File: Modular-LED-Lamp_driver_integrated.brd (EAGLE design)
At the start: 40 x 44 mm, 15 parts

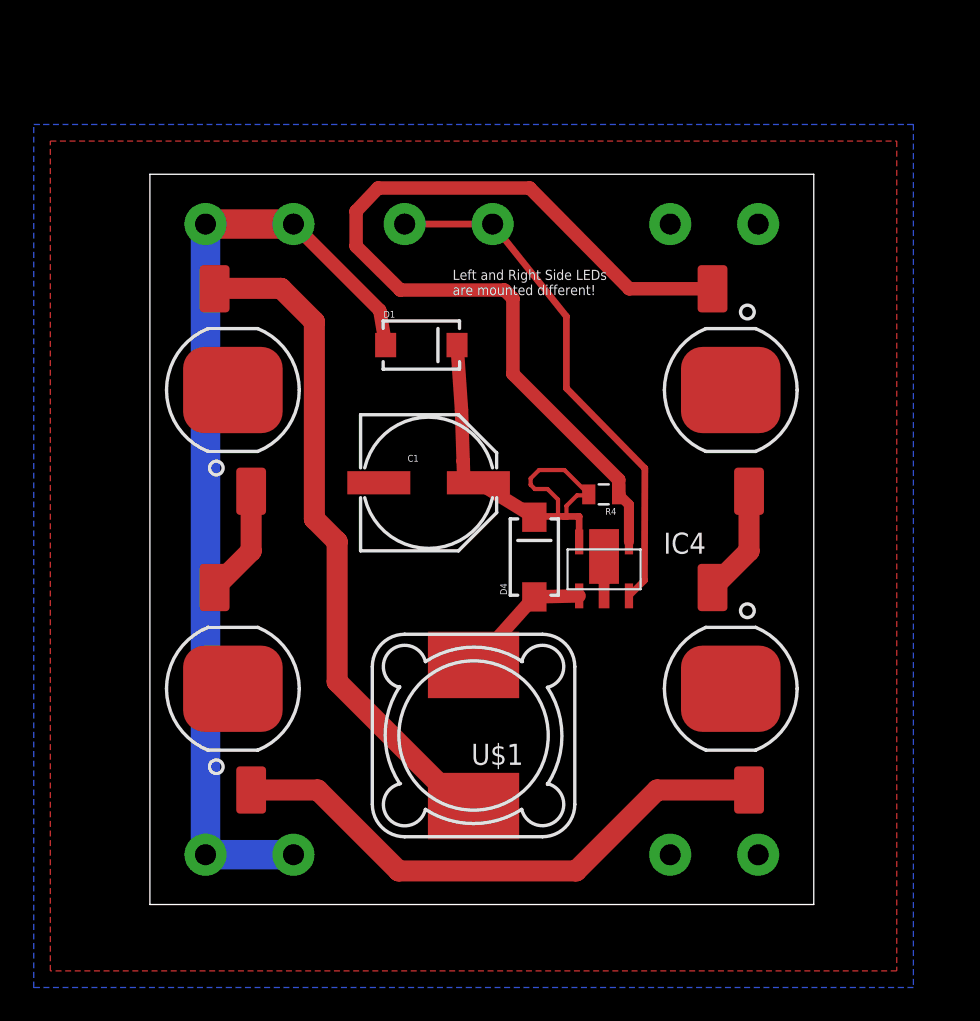
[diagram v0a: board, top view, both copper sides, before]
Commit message: changed outline to be bigger to disspate more heat, added footprint for 90° turned fuse holders, rounded edges
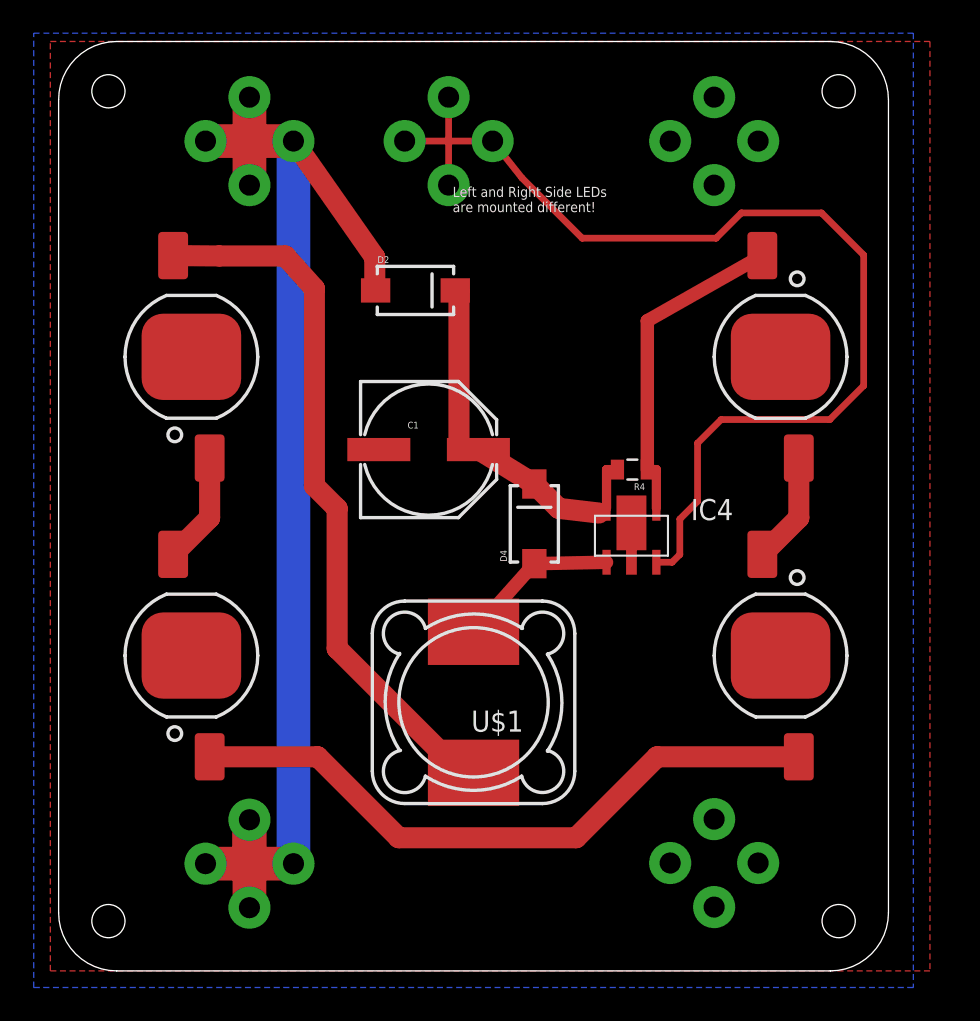
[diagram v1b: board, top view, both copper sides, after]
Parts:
- removed D1: B340A, SparkFun-DiscreteSemi:SMA-DIODE
- added D2: (no value), SparkFun-DiscreteSemi:SMA-DIODE-KIT
- added GND-CLIP1, GND-CLIP3: GND, timon-diverses:FUSE-HOLDER-5X20MM
- added PWM-CLIP1, VCC-CLIP1, VCC-CLIP3: FUSE-HOLDER-5X20MM, timon-diverses:FUSE-HOLDER-5X20MM
- R4: value 0.13 -> 0.33
- moved GND-CLIP 5.00 mm to (39.0, 47.0)
- moved PWM-CLIP 5.00 mm to (23.0, 47.0)
- moved VCC-CLIP 5.00 mm to (11.0, 47.0)
- moved LED-1 3.61 mm to (43.0, 34.0)
- moved LED-4 3.61 mm to (43.0, 16.0)
- moved LED-2 3.20 mm to (7.50, 16.0)
- moved LED-3 3.20 mm to (7.50, 34.0)
- moved IC4 2.61 mm to (32.5, 21.6)
- moved R4 2.28 mm to (34.1, 27.2)
- moved C1 2.00 mm to (21.8, 28.4)
- moved D4 2.00 mm to (28.2, 23.9)
- moved U$1 2.00 mm to (24.5, 13.2)
- moved VCC-CLIP2 0.54 mm to (11.0, 3.46)
- moved GND-CLIP2 0.50 mm to (39.0, 3.50)
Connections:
- net GND: now also GND-CLIP1.CLIP-INPUT1, GND-CLIP1.CLIP-INPUT2, GND-CLIP3.CLIP-INPUT1, GND-CLIP3.CLIP-INPUT2
- net PWM: now also PWM-CLIP1.CLIP-INPUT1, PWM-CLIP1.CLIP-INPUT2
- net VCC: now also D2.C; no longer D1.C
- net VCC-RAW: now also D2.A, VCC-CLIP1.CLIP-INPUT1, VCC-CLIP1.CLIP-INPUT2, VCC-CLIP3.CLIP-INPUT1, VCC-CLIP3.CLIP-INPUT2; no longer D1.A
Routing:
- net LED+: track 55.0 -> 19.8 mm
- net PWM: track 31.6 -> 65.4 mm
- net VCC-RAW: track 58.1 -> 78.0 mm
- net N$2: track 34.0 -> 39.5 mm
- net VCC: track 27.6 -> 23.0 mm
- net LED-: track 40.4 -> 43.0 mm
- net N$1: track 8.20 -> 9.85 mm
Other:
- board size 40 x 44 mm -> 50 x 56 mm

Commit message: updated integrated driver module to be 1W instead of 3W
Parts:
- R4: value 0.33 -> 0.3; device SparkFun-Resistors:0805 -> SparkFun-Resistors:1206
- moved R4 0.51 mm to (34.1, 27.7)
- renumbered U$1 to INDUCTOR
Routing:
- net VCC-RAW: track 78.0 -> 89.2 mm
- net LED+: track 19.8 -> 18.8 mm
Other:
- outline, holes or cut-outs redrawn
- board text added: "+"
- board text added: "-"
- board text added: "GND"
- board text added: "LED+"
- board text added: "LED-"
- board text added: "PT4115"
- board text added: "PWM"
- board text added: "Sense"
- board text added: "VCC"

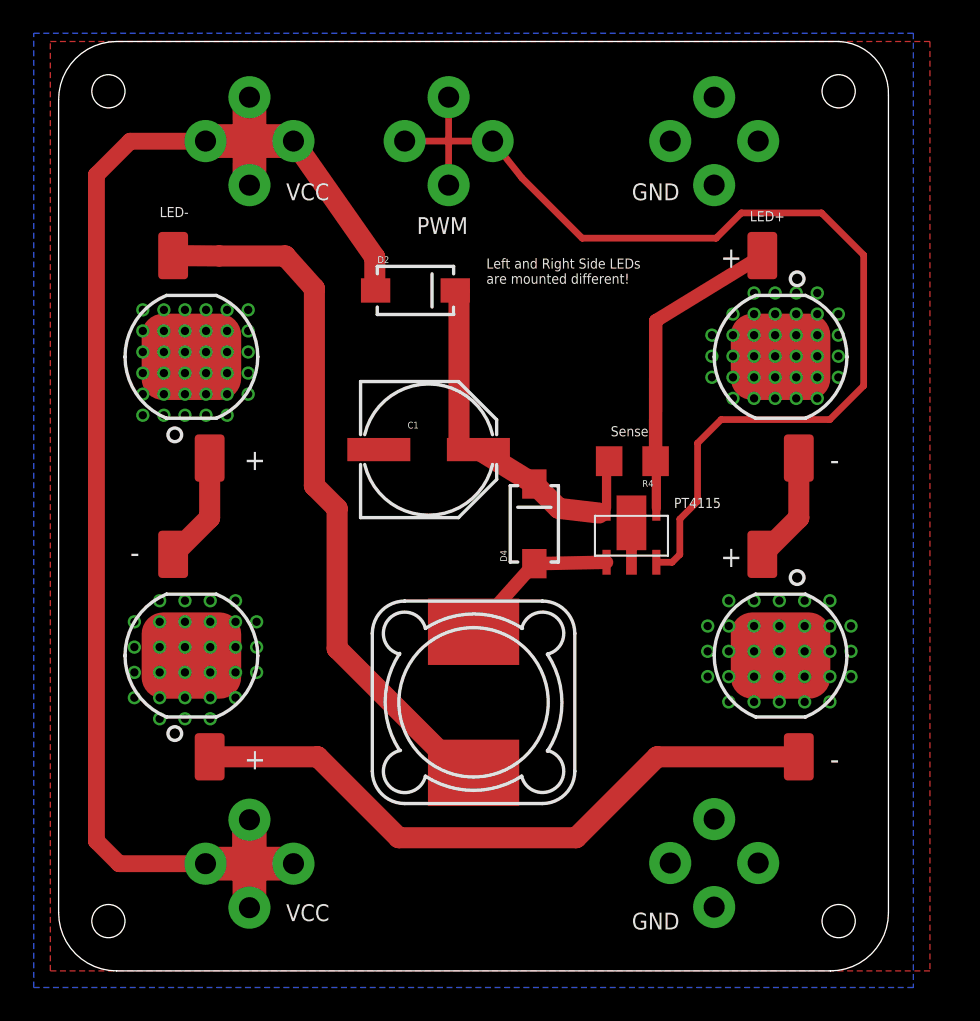
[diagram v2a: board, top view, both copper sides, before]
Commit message: fixed issued with PWM rod causing short circuit when two boards are mounted with one being reversed. Added PDF for schematic and board.
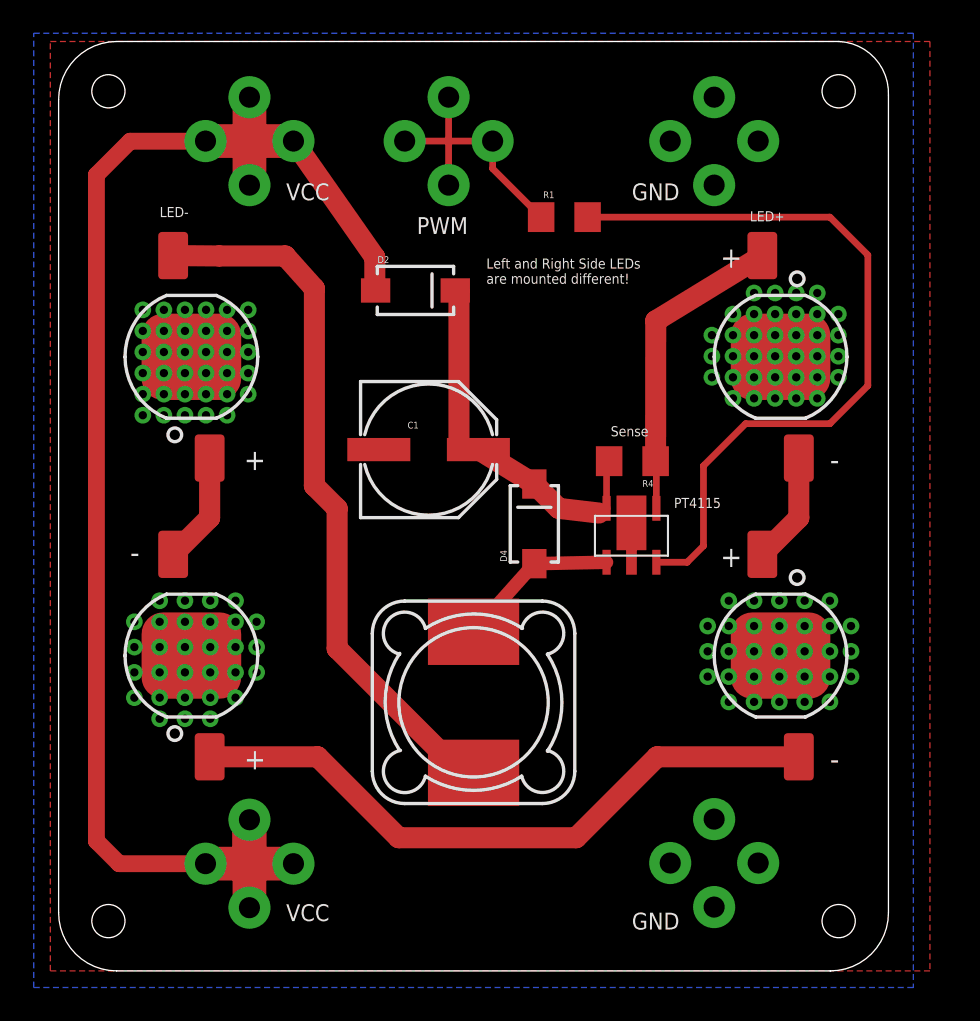
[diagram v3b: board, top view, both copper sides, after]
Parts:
- added R1: 2k, SparkFun-Resistors:1206
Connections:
- new net N$5: IC4.3, R1.2
- net PWM: now also R1.1; no longer IC4.3
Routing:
- net PWM: track 65.4 -> 16.5 mm
- net N$5: track 0.00 -> 45.7 mm

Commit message: Added BOM, updated schematic and board for integrated variant
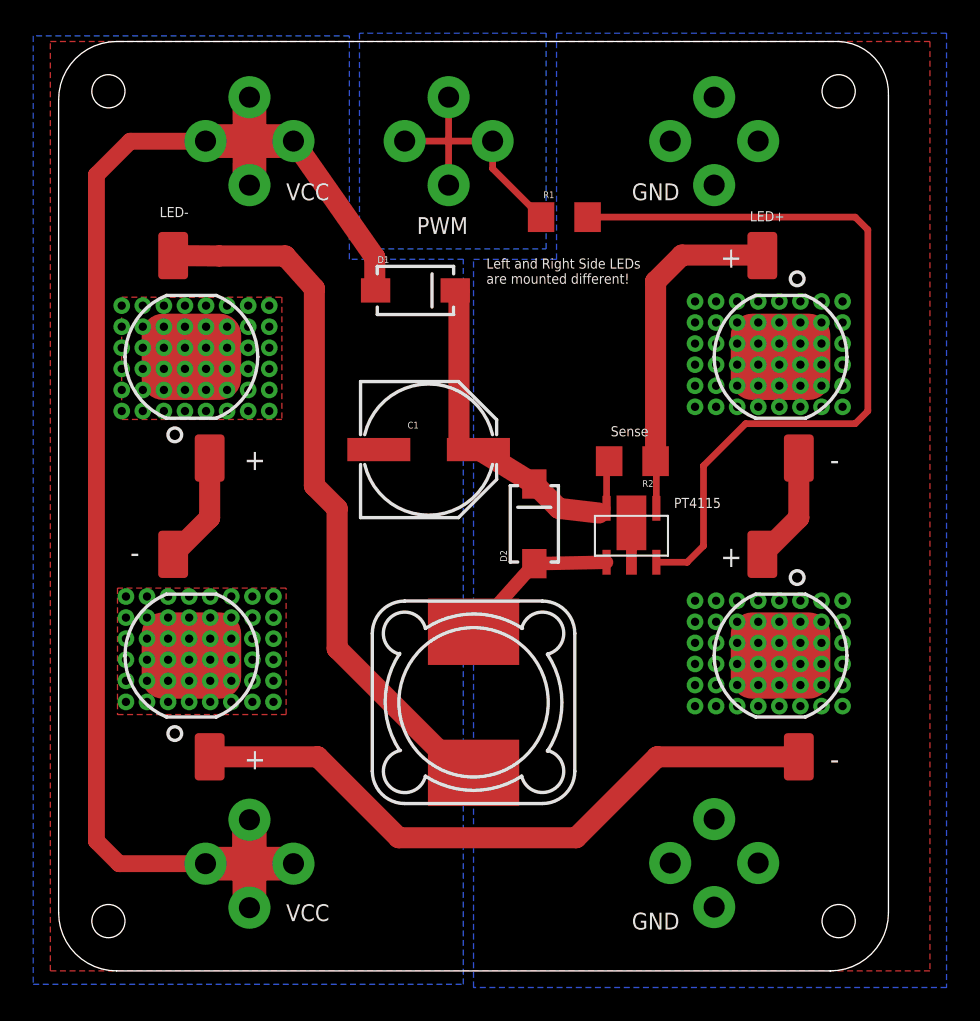
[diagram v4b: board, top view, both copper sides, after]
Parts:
- removed D4: (no value), SparkFun-DiscreteSemi:SMA-DIODE-KIT
- added D1: (no value), SparkFun-DiscreteSemi:SMA-DIODE-KIT
- GND-CLIP, GND-CLIP1, GND-CLIP2, GND-CLIP3: value GND -> FUSE-HOLDER-5X20MM
- moved D2 15.8 mm to (28.2, 23.9), turned to 90 degrees
- renumbered R4 to R2
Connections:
- net GND: no longer LED-2.S, LED-3.S
- net N$1: now also D2.A; no longer D4.A
- net VCC: now also D1.C; no longer D4.C
- net VCC-RAW: now also D1.A, LED-2.S, LED-3.S; no longer D2.A
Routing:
- net LED+: track 18.8 -> 20.8 mm
- net N$5: track 45.7 -> 47.5 mm
- net VCC-RAW: vias 0 -> 96
- added copper zone on layer 16, net PWM
- added copper zone on layer 1, net VCC-RAW
- added copper zone on layer 16, net VCC-RAW
